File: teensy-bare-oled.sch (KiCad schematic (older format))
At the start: 5 parts, among them J1 TEENSY-LC, J2 OLED_128x64

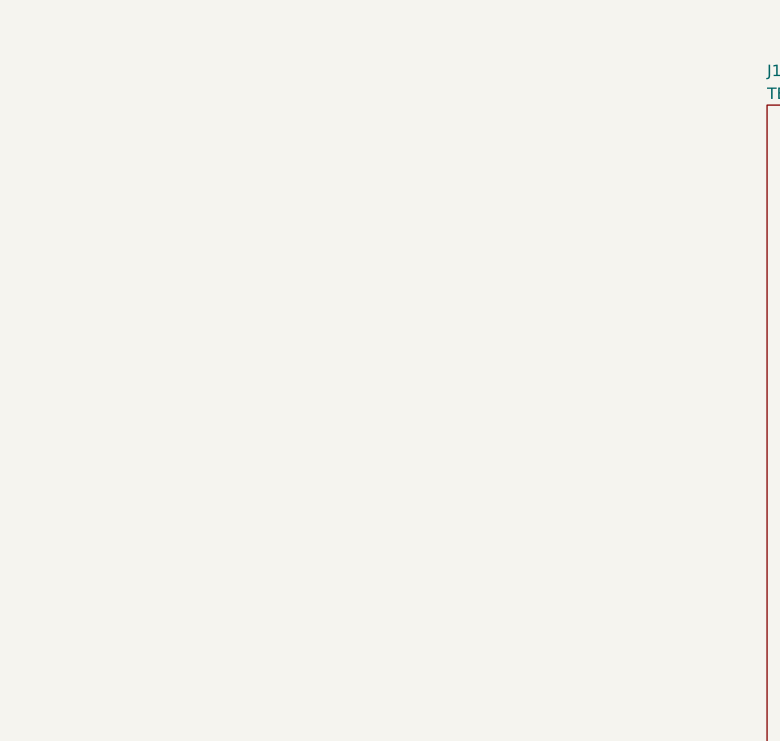
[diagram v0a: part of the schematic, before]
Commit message: create breakout for er-oled-0.91-1
from:
https://github.com/Agilack/contrib-kicad_parts/tree/master/disp-oled-EastRising

potentially for:
http://www.buydisplay.com/default/0-91-inch-128x32-oled-display-module-serial-spi-ssd1306-white-on-black
http://www.buydisplay.com/default/0-91-inch-128x32-oled-display-with-connector-fpc-ssd1306-white-on-black
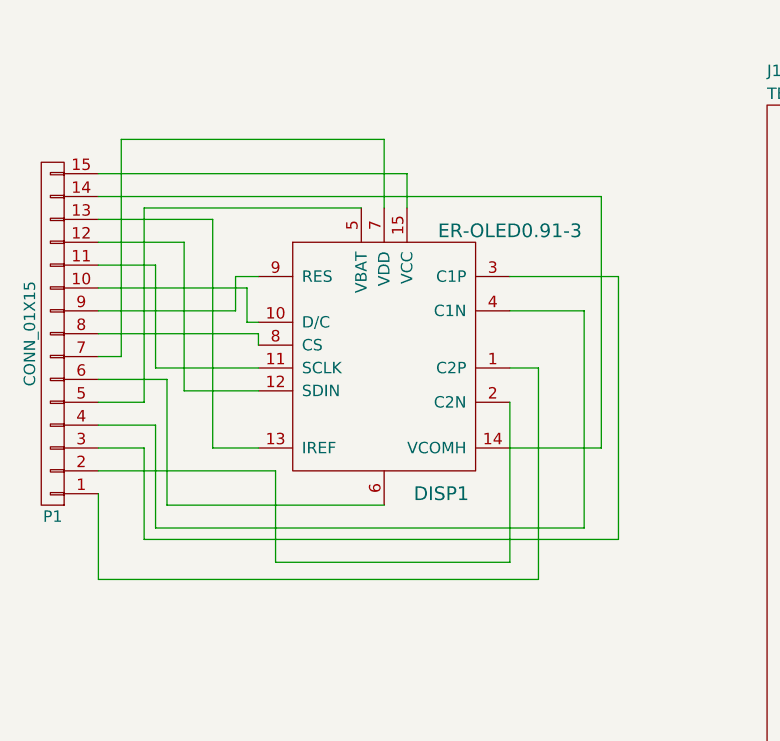
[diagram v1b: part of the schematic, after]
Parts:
- added DISP1: ER-OLED0.91-3, disp-oled-EastRising:er-oled-0.91-1, symbol ER-OLED0.91-3
- added P1: CONN_01X15, Wickerlib:CONN-HEADER-STRAIGHT-P2.54MM-1x15, symbol CONN_01X15
- CAP1, CAP2, CAP3: footprint Wickerlib:CAPSENSE_CIRCLE_D10 -> Wickerlib:CAPSENSE-CIRCLE-D10MM
- J1: footprint Wickerlib:TEENSY-LC -> Wickerlib:TEENSY-LC-SILK
- J2: footprint Wickerlib:Pin_Header_Straight_1x08 -> Wickerlib:CONN-HEADER-STRAIGHT-P2.54MM-1x08
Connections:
- new net: DISP1.1 (C2P), P1.1 (P1)
- new net: DISP1.10 (D/C), P1.10 (P10)
- new net: DISP1.11 (SCLK), P1.11 (P11)
- new net: DISP1.12 (SDIN), P1.12 (P12)
- new net: DISP1.13 (IREF), P1.13 (P13)
- new net: DISP1.14 (VCOMH), P1.14 (P14)
- new net: DISP1.15 (VCC), P1.15 (P15)
- new net: DISP1.2 (C2N), P1.2 (P2)
- new net: DISP1.3 (C1P), P1.3 (P3)
- new net: DISP1.4 (C1N), P1.4 (P4)
- new net: DISP1.5 (VBAT), P1.5 (P5)
- new net: DISP1.6, P1.6 (P6)
- new net: DISP1.7 (VDD), P1.7 (P7)
- new net: DISP1.8 (CS), P1.8 (P8)
- new net: DISP1.9 (RES), P1.9 (P9)
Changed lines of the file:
@@
 LIBS:valves
 LIBS:wickerlib
+LIBS:er-oled0.91-3
 LIBS:teensy-bare-oled-cache
 EELAYER 25 0
@@
 F 0 "J1" H 5025 4200 50  0000 L CNN
 F 1 "TEENSY-LC" H 5025 4100 50  0000 L CNN
-F 2 "Wickerlib:TEENSY-LC" V 4975 2550 50  0001 C CIN
+F 2 "Wickerlib:TEENSY-LC-SILK" V 4975 2550 50  0001 C CIN
 F 3 "https://cdn.harwin.com/pdfs/60page140.pdf" H 5275 2950 5   0001 C CNN
 F 4 "TEENSY-LC" V 4975 2550 50  0001 C CIN "Package"
@@
 F 0 "J2" H 7625 3600 50  0000 L CNN
 F 1 "OLED_128x64" H 7625 3500 50  0000 L CNN
-F 2 "Wickerlib:Pin_Header_Straight_1x08" H 7625 2800 50  0001 C CIN
+F 2 "Wickerlib:CONN-HEADER-STRAIGHT-P2.54MM-1x08" H 7625 2800 50  0001 C CIN
 F 3 "https://cdn.harwin.com/pdfs/60page140.pdf" H 7625 3150 5   0001 C CNN
 F 4 "Pin_Header_Straight_1x08" H 7625 2800 50  0001 C CIN "Package"
@@
 F 0 "CAP1" H 6900 4225 60  0000 L CNN
 F 1 "CAPSENSE_CIRCLE" H 6900 4025 60  0000 L CNN
-F 2 "Wickerlib:CAPSENSE_CIRCLE_D10" H 6650 4125 60  0001 C CNN
+F 2 "Wickerlib:CAPSENSE-CIRCLE-D10MM" H 6650 4125 60  0001 C CNN
 F 3 "" H 6650 4125 60  0000 C CNN
 	1    6650 4125
@@
 F 0 "CAP2" H 6950 4700 60  0000 L CNN
 F 1 "CAPSENSE_CIRCLE" H 6950 4500 60  0000 L CNN
-F 2 "Wickerlib:CAPSENSE_CIRCLE_D10" H 6700 4600 60  0001 C CNN
+F 2 "Wickerlib:CAPSENSE-CIRCLE-D10MM" H 6700 4600 60  0001 C CNN
 F 3 "" H 6700 4600 60  0000 C CNN
 	1    6700 4600
@@
 F 0 "CAP3" H 7200 1775 60  0000 L CNN
 F 1 "CAPSENSE_CIRCLE" H 7200 1575 60  0000 L CNN
-F 2 "Wickerlib:CAPSENSE_CIRCLE_D10" H 6950 1675 60  0001 C CNN
+F 2 "Wickerlib:CAPSENSE-CIRCLE-D10MM" H 6950 1675 60  0001 C CNN
 F 3 "" H 6950 1675 60  0000 C CNN
 	1    6950 1675
@@
 NoConn ~ 5475 5350
 NoConn ~ 5600 2650
+$Comp
+L ER-OLED0.91-3 DISP1
+U 1 1 58B66AB6
+P 3350 2950
+F 0 "DISP1" H 3600 2350 60  0000 C CNN
+F 1 "ER-OLED0.91-3" H 3900 3500 60  0000 C CNN
+F 2 "disp-oled-EastRising:er-oled-0.91-1" H 3350 2950 60  0001 C CNN
+F 3 "" H 3350 2950 60  0000 C CNN
+	1    3350 2950
+	1    0    0    -1
+$EndComp
+$Comp
+L CONN_01X15 P1
+U 1 1 58B66E93
+P 1900 2850
+F 0 "P1" H 1900 3650 50  0000 C CNN
+F 1 "CONN_01X15" V 2000 2850 50  0000 C CNN
+F 2 "Wickerlib:CONN-HEADER-STRAIGHT-P2.54MM-1x15" H 1900 2850 50  0001 C CNN
+F 3 "" H 1900 2850 50  0000 C CNN
+	1    1900 2850
+	-1   0    0    1
+$EndComp
+Wire Wire Line
+	2100 2150 3450 2150
+Wire Wire Line
+	3450 2150 3450 2300
+Wire Wire Line
+	2100 2250 4300 2250
+Wire Wire Line
+	4300 2250 4300 3350
+Wire Wire Line
+	4300 3350 3900 3350
+Wire Wire Line
+	2100 2350 2600 2350
+Wire Wire Line
+	2600 2350 2600 3350
+Wire Wire Line
+	2600 3350 2800 3350
+Wire Wire Line
+	2100 2450 2475 2450
+Wire Wire Line
+	2475 2450 2475 3100
+Wire Wire Line
+	2475 3100 2800 3100
+Wire Wire Line
+	2100 2550 2350 2550
+Wire Wire Line
+	2350 2550 2350 3000
+Wire Wire Line
+	2350 3000 2800 3000
+Wire Wire Line
+	2100 2750 2700 2750
+Wire Wire Line
+	2700 2750 2700 2600
+Wire Wire Line
+	2700 2600 2800 2600
+Wire Wire Line
+	2100 2650 2750 2650
+Wire Wire Line
+	2750 2650 2750 2800
+Wire Wire Line
+	2750 2800 2800 2800
+Wire Wire Line
+	2100 2850 2800 2850
+Wire Wire Line
+	2800 2850 2800 2900
+Wire Wire Line
+	2100 2950 2200 2950
+Wire Wire Line
+	2200 2950 2200 2000
+Wire Wire Line
+	2200 2000 3350 2000
+Wire Wire Line
+	3350 2000 3350 2300
+Wire Wire Line
+	2100 3150 2300 3150
+Wire Wire Line
+	2300 3150 2300 2300
+Wire Wire Line
+	2300 2300 3250 2300
+Wire Wire Line
+	2100 3050 2400 3050
+Wire Wire Line
+	2400 3050 2400 3600
+Wire Wire Line
+	2400 3600 3350 3600
+Wire Wire Line
+	2100 3250 2350 3250
+Wire Wire Line
+	2350 3250 2350 3700
+Wire Wire Line
+	2350 3700 4225 3700
+Wire Wire Line
+	4225 3700 4225 2750
+Wire Wire Line
+	4225 2750 3900 2750
+Wire Wire Line
+	2100 3350 2300 3350
+Wire Wire Line
+	2300 3350 2300 3750
+Wire Wire Line
+	2300 3750 4375 3750
+Wire Wire Line
+	4375 3750 4375 2600
+Wire Wire Line
+	4375 2600 3900 2600
+Wire Wire Line
+	2100 3450 2875 3450
+Wire Wire Line
+	2875 3450 2875 3850
+Wire Wire Line
+	2875 3850 3900 3850
+Wire Wire Line
+	3900 3850 3900 3150
+Wire Wire Line
+	2100 3550 2100 3925
+Wire Wire Line
+	2100 3925 4025 3925
+Wire Wire Line
+	4025 3925 4025 3000
+Wire Wire Line
+	4025 3000 3900 3000
 $EndSCHEMATC
